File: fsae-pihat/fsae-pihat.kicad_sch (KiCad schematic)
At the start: 68 parts, among them J1 Conn_02x02_Odd_Even, J2 Raspberry_Pi_4, J3 Conn_01x03_Pin, J4 1-2834011-4, J5 1-2834011-4, U1 TPS5430DDAR, U2 PCF8563T, U3 MCP2515-xST, U4 SN65HVD230DR-JSM, U5 TPS1H200AQDGNRQ1, X1 Q13FC1350000400, X2 X322512MSB4SI

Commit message: feat: readme, journal, pcb updates
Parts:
- removed D11, D12, D2, D3: SS34, Diode_SMD:D_SMA, symbol Diode:SS34
- added D11, D12, D2, D3: SS54, PCM_JLCPCB:D_SMA, symbol PCM_JLCPCB-Diodes:Schottky,SS54,(2)
- added JP2: Jumper_3_Open, Connector_PinHeader_2.54mm:PinHeader_1x03_P2.54mm_Vertical, symbol Jumper:Jumper_3_Open
- J1, J3: now left out of the parts list
- JP1: now in the parts list
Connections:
- net +20V_USB: now also D12.2
- net +24V: now also D2.1, D3.1
- net +24V-BST: now also D3.2
- net +24V-CAR: now also D11.2, D2.2, JP2.2 (C); no longer D1.2 (A2), F1.1
- net BUCK_IN: now also D11.1, D12.1
- new net 24V-RAW: D1.2 (A2), F1.1, JP2.1 (A)
- no-connect marks 32 -> 33
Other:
- moved on the sheet: D1, D4, F1, J1

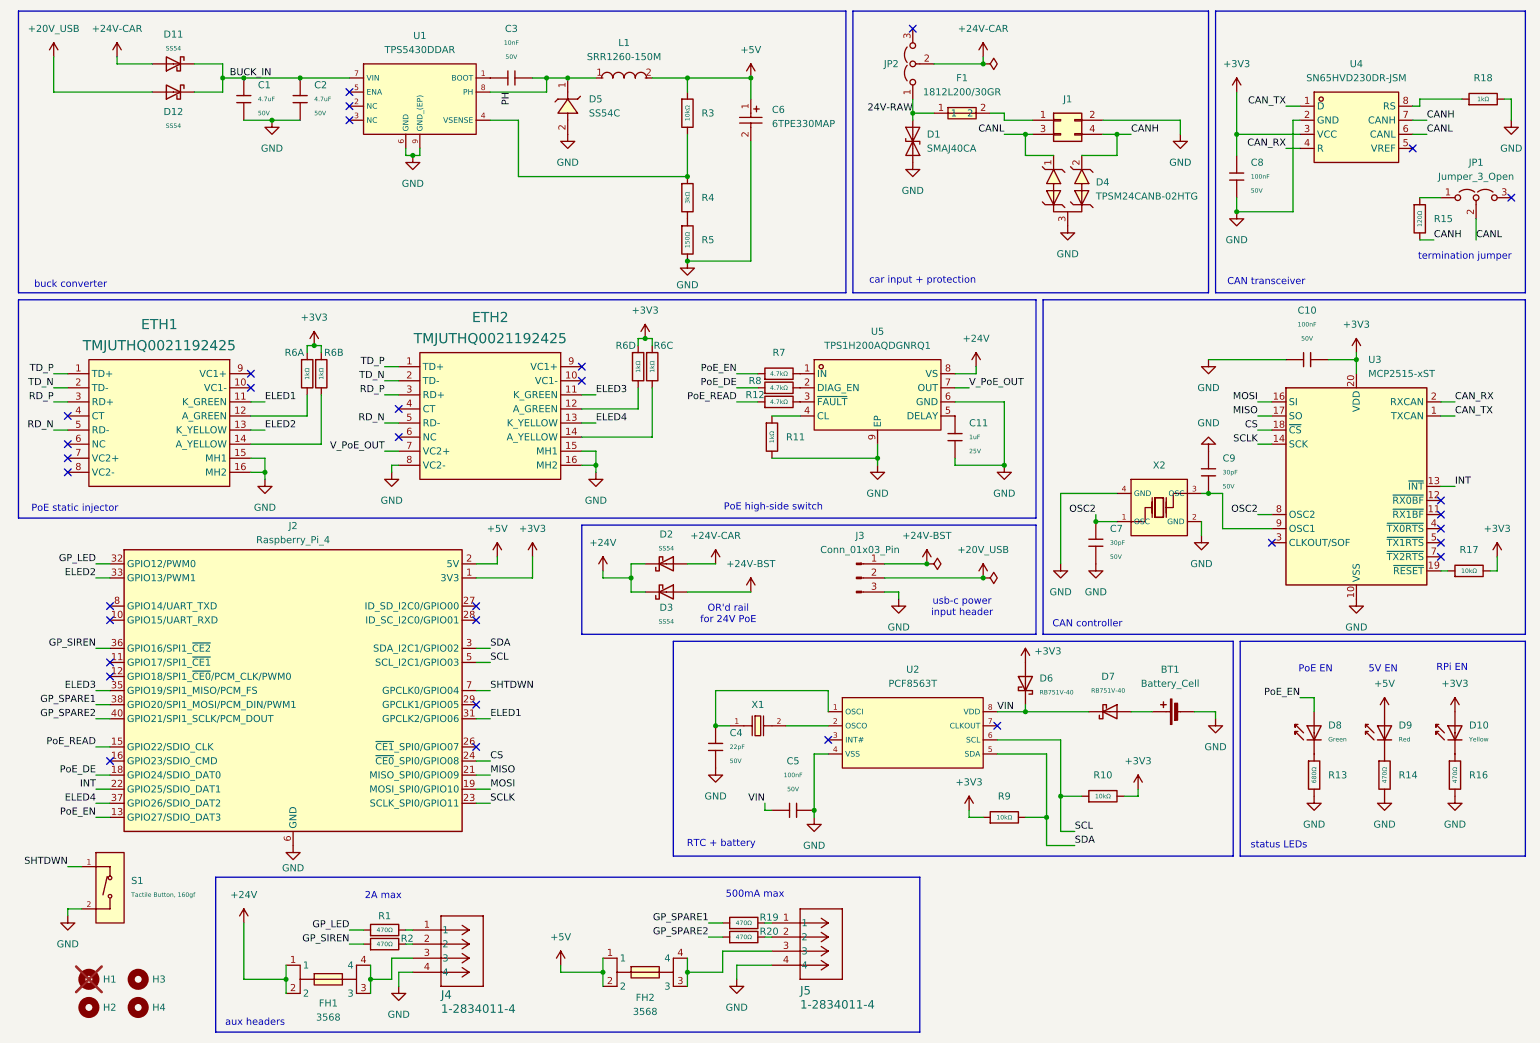
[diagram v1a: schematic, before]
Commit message: feat: pcb art and updated design
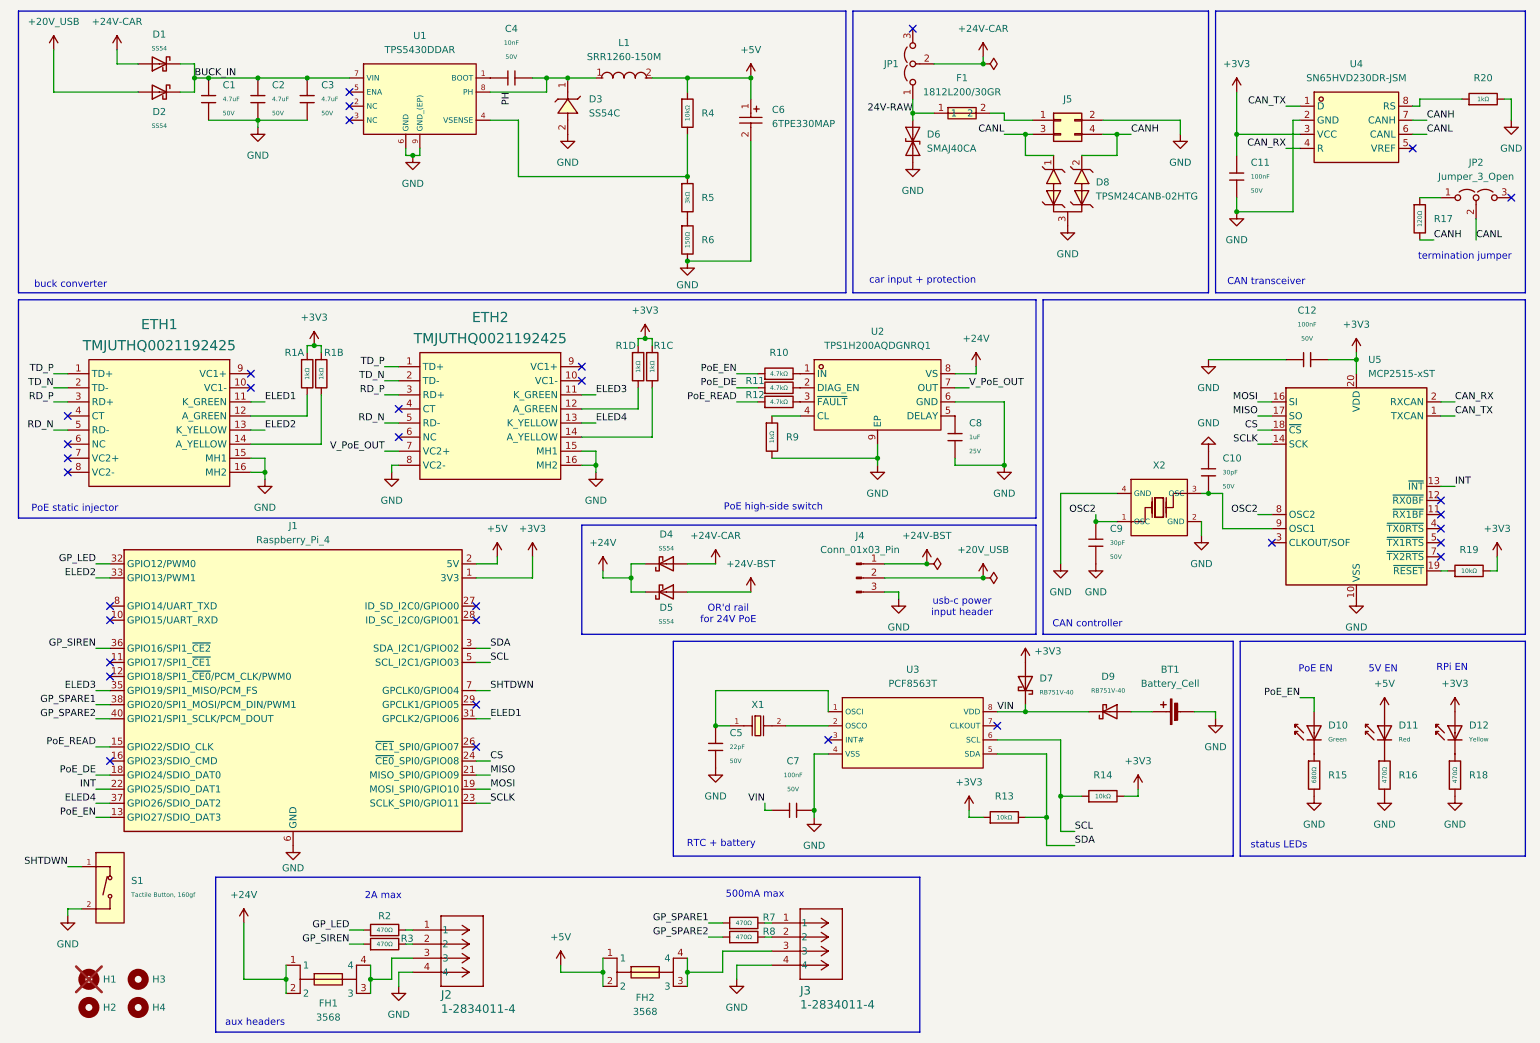
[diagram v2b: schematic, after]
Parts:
- added C3: 4.7uF, PCM_JLCPCB:C_1206, symbol PCM_JLCPCB-Capacitors:1206,4.7uF
- renumbered C9 to C10, C8 to C11, C10 to C12, C3 to C4, C4 to C5, C5 to C7, C11 to C8, C7 to C9, D11 to D1, D8 to D10, D9 to D11, D10 to D12, D12 to D2, D5 to D3, D2 to D4, D3 to D5, D1 to D6, D6 to D7, D4 to D8, D7 to D9, J2 to J1, J4 to J2, J5 to J3, J3 to J4, J1 to J5, JP2 to JP1, JP1 to JP2, R6 to R1, R7 to R10, R8 to R11, R9 to R13, R10 to R14, R13 to R15, R14 to R16, R15 to R17, R16 to R18, R17 to R19, R1 to R2, R18 to R20, R2 to R3, R3 to R4, R4 to R5, R5 to R6, R19 to R7, R20 to R8, R11 to R9, U5 to U2, U2 to U3, U3 to U5
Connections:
- net BUCK_IN: now also C3.1
- net GND: now also C3.2
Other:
- moved on the sheet: C1, C2, D1, D2

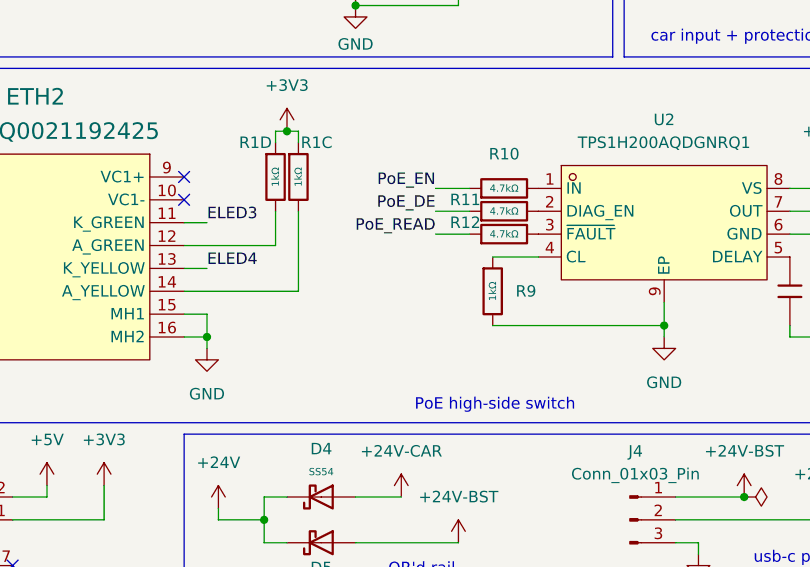
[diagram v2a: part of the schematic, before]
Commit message: fix: missed hat pullup; feat: new pd module
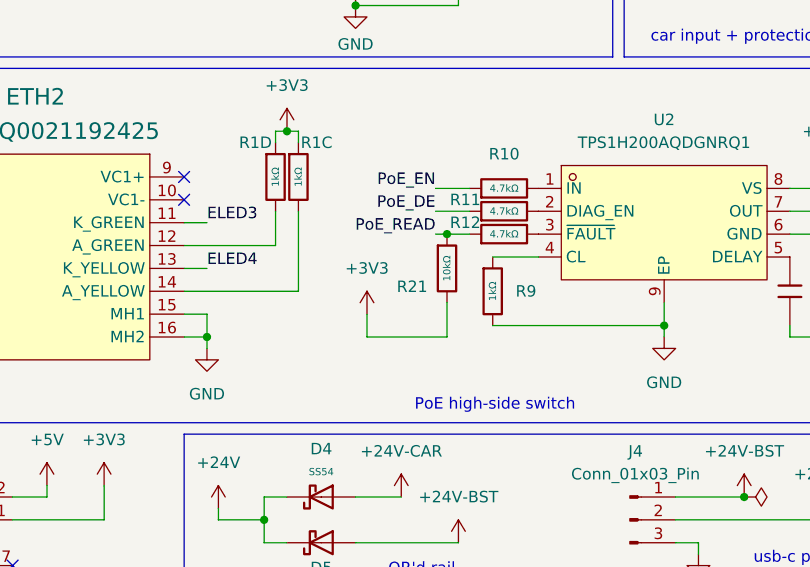
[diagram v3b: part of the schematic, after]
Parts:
- added R21: 10kΩ, PCM_JLCPCB:R_0402, symbol PCM_JLCPCB-Resistors:0402,10kΩ
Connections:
- net +3V3: now also R21.2
- net PoE_READ: now also R21.1
